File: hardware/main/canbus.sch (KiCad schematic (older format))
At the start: 21 parts, among them U201 MCP2551-I/SN, U202 MCP2515-xSO, Y201 16MHz

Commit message: Primeira versão do esquematico finalizada Falta DRC
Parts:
- U202: symbol MAB19-rescue:MCP2515-xSO-Interface_CAN_LIN -> main-rescue:MCP2515-xSO-Interface_CAN_LIN-MAB19-rescue
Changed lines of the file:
@@
 EESchema Schematic File Version 4
+LIBS:main-cache
 EELAYER 26 0
 EELAYER END
 $Descr A4 11693 8268
 encoding utf-8
-Sheet 2 7
+Sheet 2 8
 Title ""
 Date ""
@@
 Connection ~ 5550 4300
 $Comp
-L MAB19-rescue:MCP2515-xSO-Interface_CAN_LIN U202
+L main-rescue:MCP2515-xSO-Interface_CAN_LIN-MAB19-rescue U202
 U 1 1 5BE69763
 P 4300 3700

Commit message: Abstração do esquemático modificada para separar as duas placas e mostrar a conexão entre elas na folha principal
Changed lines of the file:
@@
 EESchema Schematic File Version 4
 LIBS:main-cache
-EELAYER 26 0
+EELAYER 29 0
 EELAYER END
 $Descr A4 11693 8268
 encoding utf-8
-Sheet 2 8
+Sheet 2 9
 Title ""
 Date ""
@@
 U 1 1 59FDAEE3
 P 6450 3300
-F 0 "U201" H 6050 3650 50  0000 L CNN
+F 0 "U?" H 6050 3650 50  0000 L CNN
 F 1 "MCP2551-I/SN" H 6500 2950 50  0000 L CNN
 F 2 "Package_SO:SOIC-8_3.9x4.9mm_P1.27mm" H 6450 2800 50  0001 C CIN
@@
 U 1 1 59FDAF39
 P 5200 4300
-F 0 "R203" V 5100 4250 50  0000 L CNN
+F 0 "R?" V 5100 4250 50  0000 L CNN
 F 1 "10k" V 5300 4250 50  0000 L CNN
 F 2 "Resistor_SMD:R_0805_2012Metric_Pad1.15x1.40mm_HandSolder" H 5200 4300 50  0001 C CNN
@@
 U 1 1 59FDAF40
 P 5850 3750
-F 0 "R202" H 5880 3770 50  0000 L CNN
+F 0 "R?" H 5880 3770 50  0000 L CNN
 F 1 "4k7" H 5880 3710 50  0000 L CNN
 F 2 "Resistor_SMD:R_0805_2012Metric_Pad1.15x1.40mm_HandSolder" H 5850 3750 50  0001 C CNN
@@
 U 1 1 59FDAF5C
 P 8200 3600
-F 0 "R201" V 8050 3550 50  0000 L CNN
+F 0 "R?" V 8050 3550 50  0000 L CNN
 F 1 "120" V 8100 3550 50  0000 L CNN
 F 2 "Resistor_SMD:R_0805_2012Metric_Pad1.15x1.40mm_HandSolder" H 8200 3600 50  0001 C CNN
@@
 U 1 1 5AAC0190
 P 4400 2600
-F 0 "C201" H 4410 2670 50  0000 L CNN
+F 0 "C?" H 4410 2670 50  0000 L CNN
 F 1 "100nF" H 4410 2520 50  0000 L CNN
 F 2 "Capacitor_SMD:C_0805_2012Metric_Pad1.15x1.40mm_HandSolder" H 4400 2600 50  0001 C CNN
@@
 U 1 1 5AAC0839
 P 8200 3900
-F 0 "D201" H 8200 4075 50  0000 C CNN
+F 0 "D?" H 8200 4075 50  0000 C CNN
 F 1 "pesd1can" H 8200 4000 50  0000 C CNN
 F 2 "Package_TO_SOT_SMD:SOT-23_Handsoldering" H 8050 3900 50  0001 C CNN
@@
 U 1 1 5AAC2327
 P 5550 3050
-F 0 "TP203" H 5550 3320 50  0000 C CNN
+F 0 "TP?" H 5550 3320 50  0000 C CNN
 F 1 "TXCAN" H 5550 3250 50  0000 C CNN
 F 2 "TestPoint:TestPoint_Pad_2.0x2.0mm" H 5750 3050 50  0001 C CNN
@@
 U 1 1 5AAC23CC
 P 5550 3250
-F 0 "TP204" H 5550 3520 50  0000 C CNN
+F 0 "TP?" H 5550 3520 50  0000 C CNN
 F 1 "RXCAN" H 5550 3450 50  0000 C CNN
 F 2 "TestPoint:TestPoint_Pad_2.0x2.0mm" H 5750 3250 50  0001 C CNN
@@
 U 1 1 5AAC2B03
 P 5000 3650
-F 0 "TP209" H 5000 3920 50  0000 C CNN
+F 0 "TP?" H 5000 3920 50  0000 C CNN
 F 1 "INT" H 5000 3850 50  0000 C CNN
 F 2 "TestPoint:TestPoint_Pad_2.0x2.0mm" H 5200 3650 50  0001 C CNN
@@
 U 1 1 5AAC2C42
 P 3550 3000
-F 0 "TP201" H 3550 3270 50  0000 C CNN
+F 0 "TP?" H 3550 3270 50  0000 C CNN
 F 1 "SI" H 3550 3200 50  0000 C CNN
 F 2 "TestPoint:TestPoint_Pad_2.0x2.0mm" H 3750 3000 50  0001 C CNN
@@
 U 1 1 5AAC2C8C
 P 3400 3050
-F 0 "TP202" H 3400 3320 50  0000 C CNN
+F 0 "TP?" H 3400 3320 50  0000 C CNN
 F 1 "SO" H 3400 3250 50  0000 C CNN
 F 2 "TestPoint:TestPoint_Pad_2.0x2.0mm" H 3600 3050 50  0001 C CNN
@@
 U 1 1 5AAC2CDB
 P 3100 3550
-F 0 "TP206" H 3100 3820 50  0000 C CNN
+F 0 "TP?" H 3100 3820 50  0000 C CNN
 F 1 "SCK" H 3100 3750 50  0000 C CNN
 F 2 "TestPoint:TestPoint_Pad_2.0x2.0mm" H 3300 3550 50  0001 C CNN
@@
 U 1 1 5AAC2E79
 P 3250 3450
-F 0 "TP205" H 3250 3720 50  0000 C CNN
+F 0 "TP?" H 3250 3720 50  0000 C CNN
 F 1 "SC" H 3200 3650 50  0000 C CNN
 F 2 "TestPoint:TestPoint_Pad_2.0x2.0mm" H 3450 3450 50  0001 C CNN
@@
 U 1 1 5AAC8491
 P 8800 3600
-F 0 "TP208" V 8700 3700 50  0000 C CNN
+F 0 "TP?" V 8700 3700 50  0000 C CNN
 F 1 "CAN_L" V 8800 3900 50  0000 C CNN
 F 2 "TestPoint:TestPoint_Pad_2.0x2.0mm" H 9000 3600 50  0001 C CNN
@@
 U 1 1 5AAC8C25
 P 7600 3600
-F 0 "TP207" V 7500 3700 50  0000 C CNN
+F 0 "TP?" V 7500 3700 50  0000 C CNN
 F 1 "CAN_H" V 7600 3900 50  0000 C CNN
 F 2 "TestPoint:TestPoint_Pad_2.0x2.0mm" H 7800 3600 50  0001 C CNN
@@
 AR Path="/5AABFC1B/5BE72790" Ref="Y201"  Part="1"
 AR Path="/5BE72790" Ref="Y201"  Part="1"
-F 0 "Y201" H 3150 4150 50  0000 C CNN
+F 0 "Y?" H 3150 4150 50  0000 C CNN
 F 1 "16MHz" H 3150 3950 50  0000 C CNN
 F 2 "Crystal:Crystal_HC49-U_Vertical" H 3150 4050 50  0001 C CNN
@@
 AR Path="/5AABFC1B/5BE72797" Ref="C203"  Part="1"
 AR Path="/5BE72797" Ref="C203"  Part="1"
-F 0 "C203" H 2910 4320 50  0000 L CNN
+F 0 "C?" H 2910 4320 50  0000 L CNN
 F 1 "22pF" H 2910 4170 50  0000 L CNN
 F 2 "Capacitor_SMD:C_0805_2012Metric_Pad1.15x1.40mm_HandSolder" H 2900 4250 50  0001 C CNN
@@
 AR Path="/5AABFC1B/5BE7279E" Ref="C204"  Part="1"
 AR Path="/5BE7279E" Ref="C204"  Part="1"
-F 0 "C204" H 3300 4350 50  0000 L CNN
+F 0 "C?" H 3300 4350 50  0000 L CNN
 F 1 "22pF" H 3200 4150 50  0000 L CNN
 F 2 "Capacitor_SMD:C_0805_2012Metric_Pad1.15x1.40mm_HandSolder" H 3400 4250 50  0001 C CNN
@@
 AR Path="/5AABFC1B/5BE727B2" Ref="#PWR0210"  Part="1"
 AR Path="/5BE727B2" Ref="#PWR0210"  Part="1"
-F 0 "#PWR0210" H 3150 4300 50  0001 C CNN
+F 0 "#PWR?" H 3150 4300 50  0001 C CNN
 F 1 "GND" H 3200 4350 50  0000 C CNN
 F 2 "" H 3150 4550 50  0001 C CNN
@@
 AR Path="/5AABFC1B/5BE91DED" Ref="#PWR0204"  Part="1"
 AR Path="/5BE91DED" Ref="#PWR0204"  Part="1"
-F 0 "#PWR0204" H 4400 2500 50  0001 C CNN
+F 0 "#PWR?" H 4400 2500 50  0001 C CNN
 F 1 "GND" H 4450 2550 50  0000 C CNN
 F 2 "" H 4400 2750 50  0001 C CNN
@@
 U 1 1 5BEC2EC3
 P 4300 2350
-F 0 "#PWR0201" H 4300 2200 50  0001 C CNN
+F 0 "#PWR?" H 4300 2200 50  0001 C CNN
 F 1 "+5V" H 4350 2550 50  0000 C CNN
 F 2 "" H 4300 2350 50  0001 C CNN
@@
 U 1 1 5BEDED38
 P 6550 2600
-F 0 "C202" H 6560 2670 50  0000 L CNN
+F 0 "C?" H 6560 2670 50  0000 L CNN
 F 1 "100nF" H 6560 2520 50  0000 L CNN
 F 2 "Capacitor_SMD:C_0805_2012Metric_Pad1.15x1.40mm_HandSolder" H 6550 2600 50  0001 C CNN
@@
 AR Path="/5AABFC1B/5BEDED40" Ref="#PWR0205"  Part="1"
 AR Path="/5BEDED40" Ref="#PWR0205"  Part="1"
-F 0 "#PWR0205" H 6550 2500 50  0001 C CNN
+F 0 "#PWR?" H 6550 2500 50  0001 C CNN
 F 1 "GND" H 6600 2550 50  0000 C CNN
 F 2 "" H 6550 2750 50  0001 C CNN
@@
 U 1 1 5BEDED46
 P 6450 2350
-F 0 "#PWR0202" H 6450 2200 50  0001 C CNN
+F 0 "#PWR?" H 6450 2200 50  0001 C CNN
 F 1 "+5V" H 6500 2550 50  0000 C CNN
 F 2 "" H 6450 2350 50  0001 C CNN
@@
 U 1 1 5BEE3281
 P 2200 2550
-F 0 "#PWR0203" H 2200 2400 50  0001 C CNN
+F 0 "#PWR?" H 2200 2400 50  0001 C CNN
 F 1 "+5V" H 2250 2750 50  0000 C CNN
 F 2 "" H 2200 2550 50  0001 C CNN
@@
 AR Path="/5AABFC1B/5BEE701B" Ref="#PWR0206"  Part="1"
 AR Path="/5BEE701B" Ref="#PWR0206"  Part="1"
-F 0 "#PWR0206" H 2200 2650 50  0001 C CNN
+F 0 "#PWR?" H 2200 2650 50  0001 C CNN
 F 1 "GND" H 2250 2700 50  0000 C CNN
 F 2 "" H 2200 2900 50  0001 C CNN
@@
 AR Path="/5AABFC1B/5BEE915D" Ref="#PWR0211"  Part="1"
 AR Path="/5BEE915D" Ref="#PWR0211"  Part="1"
-F 0 "#PWR0211" H 4300 4350 50  0001 C CNN
+F 0 "#PWR?" H 4300 4350 50  0001 C CNN
 F 1 "GND" H 4350 4400 50  0000 C CNN
 F 2 "" H 4300 4600 50  0001 C CNN
@@
 AR Path="/5AABFC1B/5BEE919A" Ref="#PWR0207"  Part="1"
 AR Path="/5BEE919A" Ref="#PWR0207"  Part="1"
-F 0 "#PWR0207" H 6450 3850 50  0001 C CNN
+F 0 "#PWR?" H 6450 3850 50  0001 C CNN
 F 1 "GND" H 6500 3900 50  0000 C CNN
 F 2 "" H 6450 4100 50  0001 C CNN
@@
 U 1 1 5BEF6349
 P 5550 4500
-F 0 "C205" H 5560 4570 50  0000 L CNN
+F 0 "C?" H 5560 4570 50  0000 L CNN
 F 1 "100nF" H 5560 4420 50  0000 L CNN
 F 2 "Capacitor_SMD:C_0805_2012Metric_Pad1.15x1.40mm_HandSolder" H 5550 4500 50  0001 C CNN
@@
 AR Path="/5AABFC1B/5BEFA640" Ref="#PWR0212"  Part="1"
 AR Path="/5BEFA640" Ref="#PWR0212"  Part="1"
-F 0 "#PWR0212" H 5550 4450 50  0001 C CNN
+F 0 "#PWR?" H 5550 4450 50  0001 C CNN
 F 1 "GND" H 5600 4500 50  0000 C CNN
 F 2 "" H 5550 4700 50  0001 C CNN
@@
 AR Path="/5AABFC1B/5BF0D416" Ref="#PWR0208"  Part="1"
 AR Path="/5BF0D416" Ref="#PWR0208"  Part="1"
-F 0 "#PWR0208" H 8200 3900 50  0001 C CNN
+F 0 "#PWR?" H 8200 3900 50  0001 C CNN
 F 1 "GND" H 8250 3950 50  0000 C CNN
 F 2 "" H 8200 4150 50  0001 C CNN
@@
 U 1 1 5BEBB382
 P 5550 4150
-F 0 "#PWR0107" H 5550 4000 50  0001 C CNN
+F 0 "#PWR?" H 5550 4000 50  0001 C CNN
 F 1 "+5V" H 5600 4350 50  0000 C CNN
 F 2 "" H 5550 4150 50  0001 C CNN
@@
 AR Path="/5BE69763" Ref="U202"  Part="1"
 AR Path="/5AABFC1B/5BE69763" Ref="U202"  Part="1"
-F 0 "U202" H 3850 4450 50  0000 C CNN
+F 0 "U?" H 3850 4450 50  0000 C CNN
 F 1 "MCP2515-xSO" H 4650 2950 50  0000 C CNN
 F 2 "Package_SO:SOIC-18W_7.5x11.6mm_P1.27mm" H 4300 2800 50  0001 C CIN

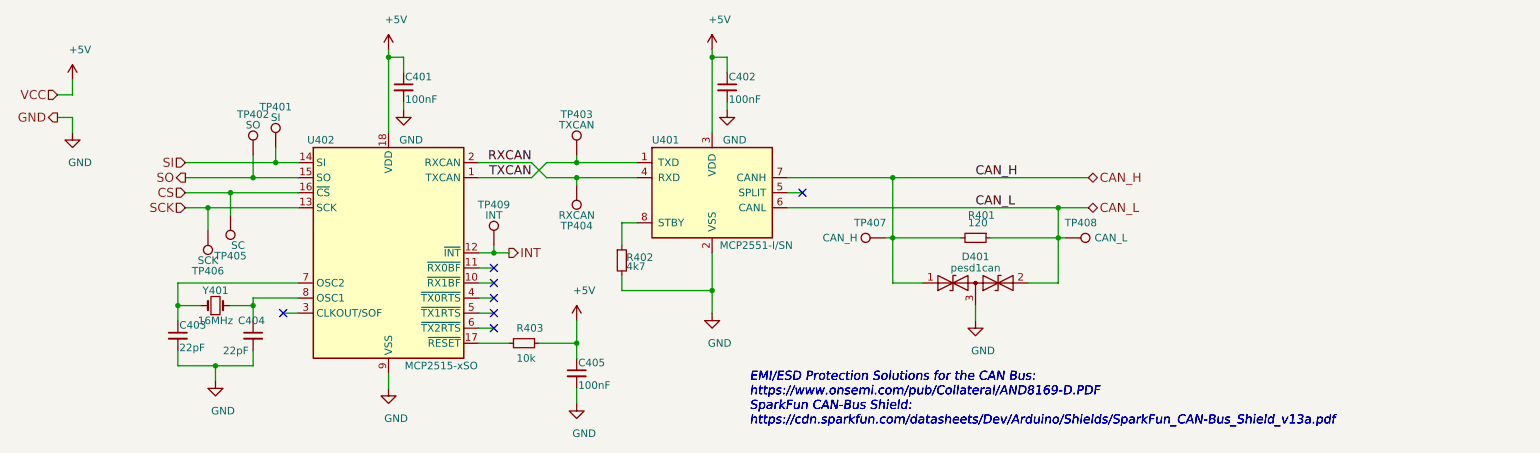
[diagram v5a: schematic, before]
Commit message: Esquematico primeira versão Erro de referencia dos componentes na PCB com os do Esquematico solucionados
Pontos de teste adicionados
Alimentar o analog com +12V
Adicionar Snubber para os reles
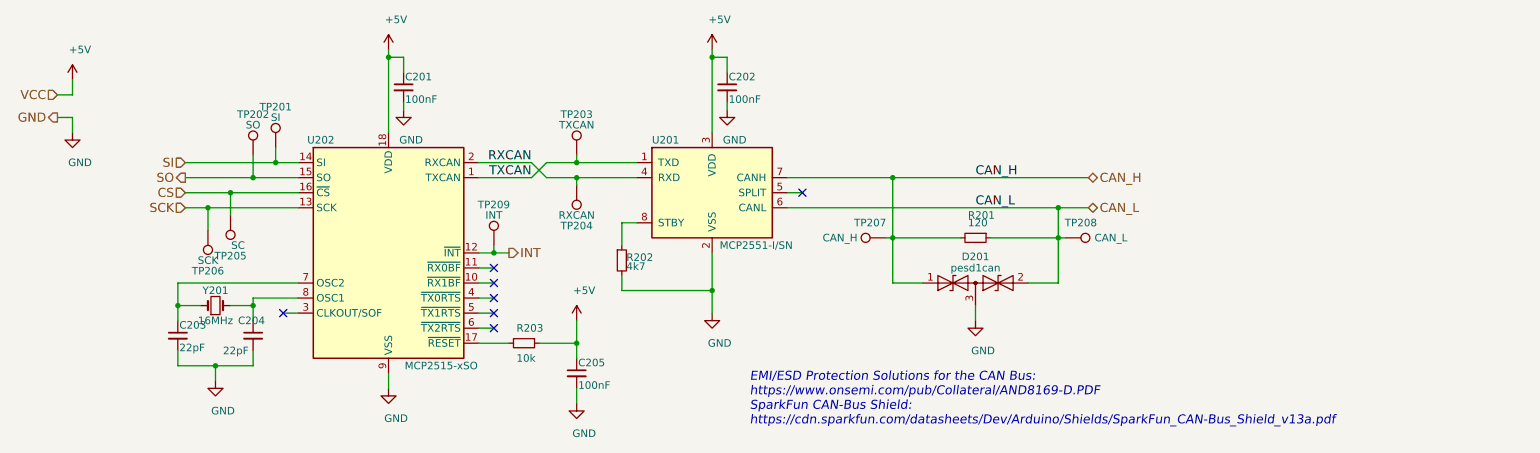
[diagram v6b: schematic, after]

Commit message: Circuito ampop incompleto
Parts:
- TP201, TP202, TP203, TP204, TP205, TP206, TP207, TP208, TP209: footprint TestPoint:TestPoint_Pad_2.0x2.0mm -> TestPoint:TestPoint_Pad_D1.5mm
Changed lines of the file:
@@
 F 0 "TP203" H 5550 3320 50  0000 C CNN
 F 1 "TXCAN" H 5550 3250 50  0000 C CNN
-F 2 "TestPoint:TestPoint_Pad_2.0x2.0mm" H 5750 3050 50  0001 C CNN
+F 2 "TestPoint:TestPoint_Pad_D1.5mm" H 5750 3050 50  0001 C CNN
 F 3 "" H 5750 3050 50  0001 C CNN
 	1    5550 3050
@@
 F 0 "TP204" H 5550 3520 50  0000 C CNN
 F 1 "RXCAN" H 5550 3450 50  0000 C CNN
-F 2 "TestPoint:TestPoint_Pad_2.0x2.0mm" H 5750 3250 50  0001 C CNN
+F 2 "TestPoint:TestPoint_Pad_D1.5mm" H 5750 3250 50  0001 C CNN
 F 3 "" H 5750 3250 50  0001 C CNN
 	1    5550 3250
@@
 F 0 "TP209" H 5000 3920 50  0000 C CNN
 F 1 "INT" H 5000 3850 50  0000 C CNN
-F 2 "TestPoint:TestPoint_Pad_2.0x2.0mm" H 5200 3650 50  0001 C CNN
+F 2 "TestPoint:TestPoint_Pad_D1.5mm" H 5200 3650 50  0001 C CNN
 F 3 "" H 5200 3650 50  0001 C CNN
 	1    5000 3650
@@
 F 0 "TP201" H 3550 3270 50  0000 C CNN
 F 1 "SI" H 3550 3200 50  0000 C CNN
-F 2 "TestPoint:TestPoint_Pad_2.0x2.0mm" H 3750 3000 50  0001 C CNN
+F 2 "TestPoint:TestPoint_Pad_D1.5mm" H 3750 3000 50  0001 C CNN
 F 3 "" H 3750 3000 50  0001 C CNN
 	1    3550 3000
@@
 F 0 "TP202" H 3400 3320 50  0000 C CNN
 F 1 "SO" H 3400 3250 50  0000 C CNN
-F 2 "TestPoint:TestPoint_Pad_2.0x2.0mm" H 3600 3050 50  0001 C CNN
+F 2 "TestPoint:TestPoint_Pad_D1.5mm" H 3600 3050 50  0001 C CNN
 F 3 "" H 3600 3050 50  0001 C CNN
 	1    3400 3050
@@
 F 0 "TP206" H 3100 3820 50  0000 C CNN
 F 1 "SCK" H 3100 3750 50  0000 C CNN
-F 2 "TestPoint:TestPoint_Pad_2.0x2.0mm" H 3300 3550 50  0001 C CNN
+F 2 "TestPoint:TestPoint_Pad_D1.5mm" H 3300 3550 50  0001 C CNN
 F 3 "" H 3300 3550 50  0001 C CNN
 	1    3100 3550
@@
 F 0 "TP205" H 3250 3720 50  0000 C CNN
 F 1 "SC" H 3200 3650 50  0000 C CNN
-F 2 "TestPoint:TestPoint_Pad_2.0x2.0mm" H 3450 3450 50  0001 C CNN
+F 2 "TestPoint:TestPoint_Pad_D1.5mm" H 3450 3450 50  0001 C CNN
 F 3 "" H 3450 3450 50  0001 C CNN
 	1    3250 3450
@@
 F 0 "TP208" V 8700 3700 50  0000 C CNN
 F 1 "CAN_L" V 8800 3900 50  0000 C CNN
-F 2 "TestPoint:TestPoint_Pad_2.0x2.0mm" H 9000 3600 50  0001 C CNN
+F 2 "TestPoint:TestPoint_Pad_D1.5mm" H 9000 3600 50  0001 C CNN
 F 3 "" H 9000 3600 50  0001 C CNN
 	1    8800 3600
@@
 F 0 "TP207" V 7500 3700 50  0000 C CNN
 F 1 "CAN_H" V 7600 3900 50  0000 C CNN
-F 2 "TestPoint:TestPoint_Pad_2.0x2.0mm" H 7800 3600 50  0001 C CNN
+F 2 "TestPoint:TestPoint_Pad_D1.5mm" H 7800 3600 50  0001 C CNN
 F 3 "" H 7800 3600 50  0001 C CNN
 	1    7600 3600
